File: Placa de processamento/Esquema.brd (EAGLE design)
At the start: 145.1 x 89.8 mm, 12 parts

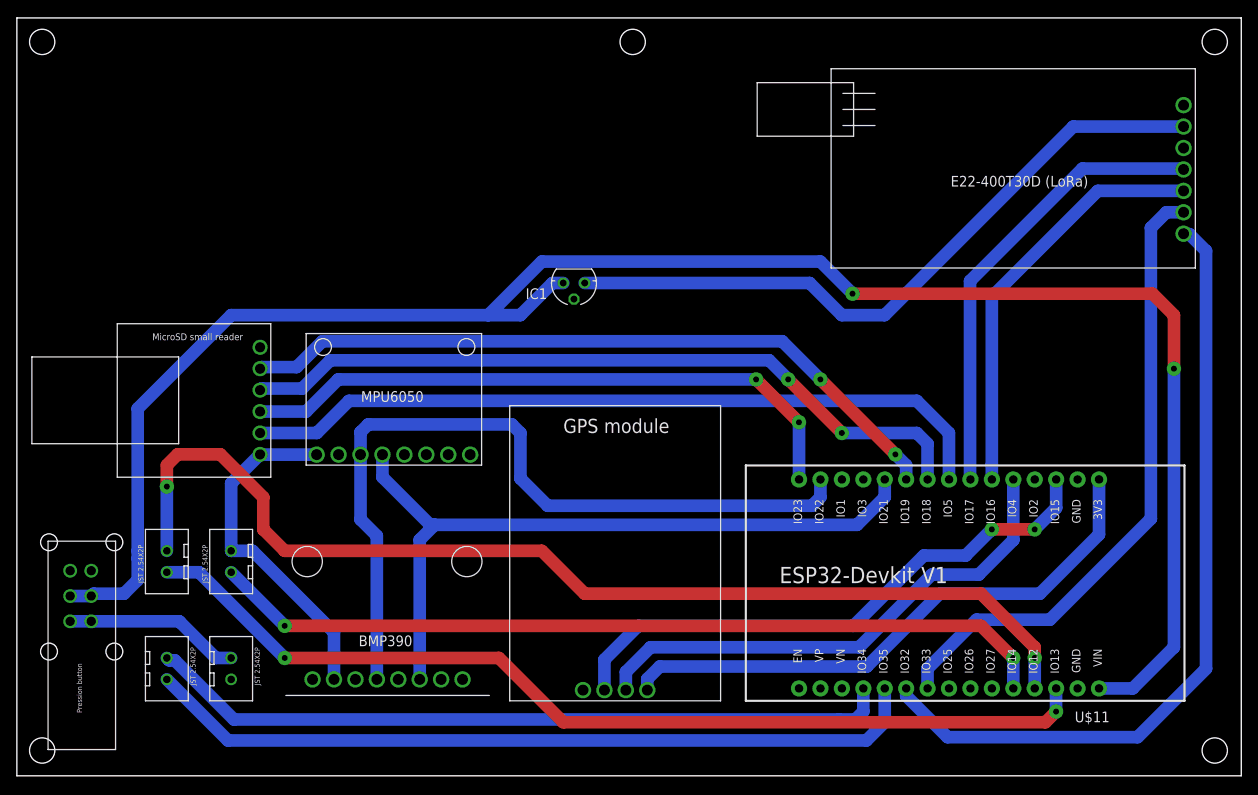
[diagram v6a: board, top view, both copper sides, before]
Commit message: Ajuste de trilhas, furos e posicionamento.
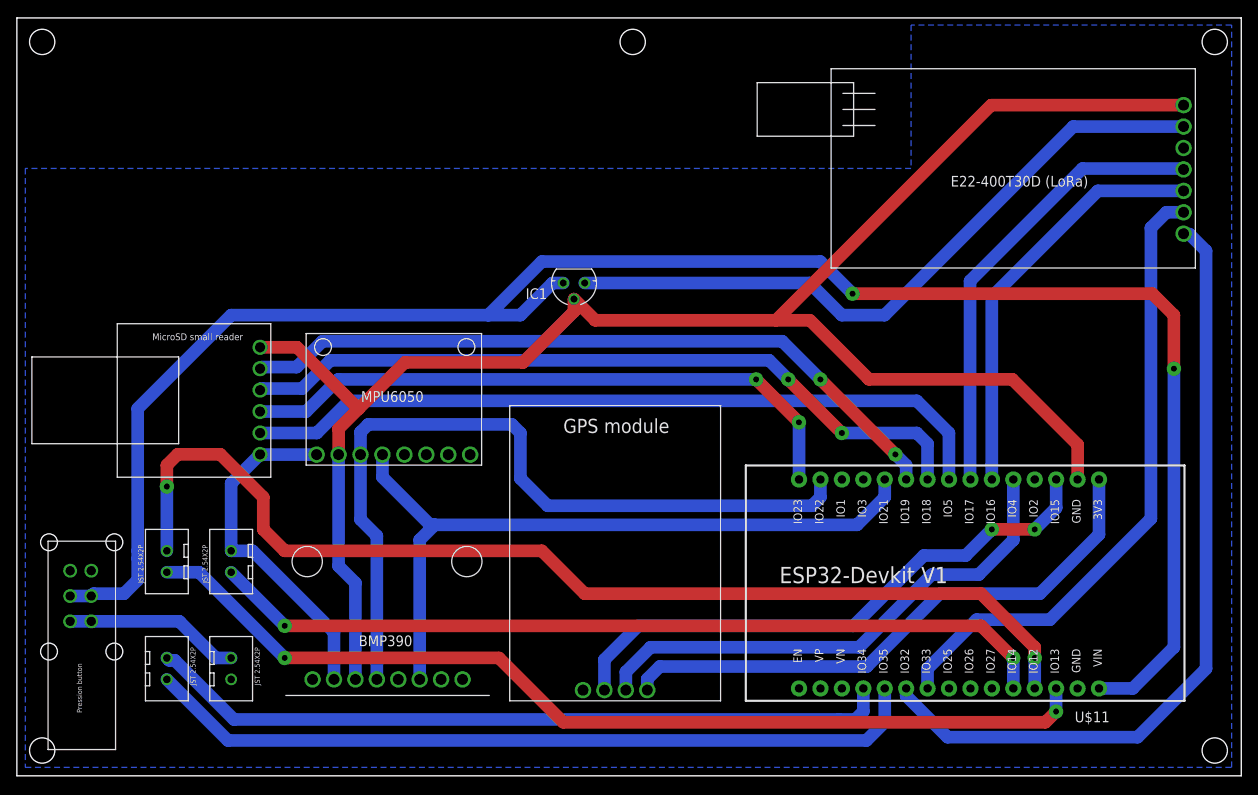
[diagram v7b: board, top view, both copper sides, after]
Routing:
- net N$4: track 0.00 -> 210.2 mm
- added copper zone on layer 16, net GND
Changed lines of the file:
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@@
 <wire x1="145.141" y1="89.84" x2="0" y2="89.84" width="0" layer="20"/>
 <wire x1="0" y1="89.84" x2="0" y2="0" width="0" layer="20"/>
-<dimension x1="0" y1="-3.81" x2="145.161" y2="-3.81" x3="72.5805" y3="-7.62" textsize="1.778" layer="27"/>
-<dimension x1="-2.54" y1="0" x2="-2.54" y2="90.17" x3="-5.08" y3="45.085" textsize="1.778" layer="47"/>
 <hole x="142" y="87" drill="3"/>
 <hole x="142" y="3" drill="3"/>
@@
 <hole x="3" y="87" drill="3"/>
 <hole x="73" y="87" drill="3"/>
+<dimension x1="0" y1="89.84" x2="0" y2="0" x3="-6" y3="44.92" textsize="1.778" layer="21" dtype="vertical"/>
+<dimension x1="0" y1="0" x2="145.141" y2="0" x3="72.5705" y3="-9" textsize="1.778" layer="21" dtype="vertical"/>
 </plain>
 <attributes>
@@
 <contactref element="U$8" pad="GND"/>
 <contactref element="U$2" pad="GND"/>
-<wire x1="125.74" y1="35.13" x2="138.303" y2="79.502" width="0" layer="19" extent="1-1"/>
-<wire x1="66.04" y1="56.515" x2="125.74" y2="35.13" width="0" layer="19" extent="1-1"/>
-<wire x1="38.1355" y1="38.0755" x2="66.04" y2="56.515" width="0" layer="19" extent="1-1"/>
-<wire x1="28.829" y1="50.8" x2="38.1355" y2="38.0755" width="0" layer="19" extent="1-1"/>
-<wire x1="40.132" y1="11.43" x2="38.1355" y2="38.0755" width="0" layer="19" extent="1-1"/>
-<wire x1="67.11" y1="10.16" x2="40.132" y2="11.43" width="0" layer="19" extent="1-1"/>
+<wire x1="66.04" y1="56.515" x2="68.555" y2="54" width="1.5" layer="1"/>
+<wire x1="101" y1="47" x2="118" y2="47" width="1.5" layer="1"/>
+<wire x1="118" y1="47" x2="125.74" y2="39.26" width="1.5" layer="1"/>
+<wire x1="125.74" y1="39.26" x2="125.74" y2="35.13" width="1.5" layer="1"/>
+<wire x1="68.555" y1="54" x2="90" y2="54" width="1.5" layer="1"/>
+<wire x1="90" y1="54" x2="94" y2="54" width="1.5" layer="1"/>
+<wire x1="94" y1="54" x2="101" y2="47" width="1.5" layer="1"/>
+<wire x1="138.303" y1="79.502" x2="115.502" y2="79.502" width="1.5" layer="1"/>
+<wire x1="115.502" y1="79.502" x2="90" y2="54" width="1.5" layer="1"/>
+<wire x1="38.1355" y1="38.0755" x2="38.1355" y2="41.1355" width="1.5" layer="1"/>
+<wire x1="46" y1="49" x2="60" y2="49" width="1.5" layer="1"/>
+<wire x1="60" y1="49" x2="66.04" y2="55.04" width="1.5" layer="1"/>
+<wire x1="66.04" y1="55.04" x2="66.04" y2="56.515" width="1.5" layer="1"/>
+<wire x1="38.1355" y1="41.1355" x2="40.5" y2="43.5" width="1.5" layer="1"/>
+<wire x1="40.5" y1="43.5" x2="46" y2="49" width="1.5" layer="1"/>
+<wire x1="28.829" y1="50.8" x2="33.2" y2="50.8" width="1.5" layer="1"/>
+<wire x1="33.2" y1="50.8" x2="40.5" y2="43.5" width="1.5" layer="1"/>
+<wire x1="38.1355" y1="38.0755" x2="38.1355" y2="24.8645" width="1.5" layer="16"/>
+<wire x1="40.132" y1="22.868" x2="40.132" y2="11.43" width="1.5" layer="16"/>
+<wire x1="38.1355" y1="24.8645" x2="40.132" y2="22.868" width="1.5" layer="16"/>
+<wire x1="40.132" y1="11.43" x2="67.11" y2="10.16" width="0" layer="19" extent="1-1"/>
 </signal>
 <signal name="N$5">
@@
 <contactref element="U$11" pad="29"/>
 <contactref element="U$7" pad="2"/>
+<polygon width="1.5" layer="16">
+<vertex x="1" y="1"/>
+<vertex x="144" y="1"/>
+<vertex x="144" y="89"/>
+<vertex x="106" y="89"/>
+<vertex x="106" y="72"/>
+<vertex x="1" y="72"/>
+</polygon>
 <wire x1="25.4" y1="11.43" x2="125.74" y2="10.36" width="0" layer="19" extent="1-1"/>
 </signal>

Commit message: Ajustes na PCB finalizados!
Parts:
- moved U$10 1.00 mm to (8.62, 16.5)
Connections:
- removed net N$4: IC1.GND, U$1.GND, U$11.2, U$2.GND, U$3.GND, U$8.GND, U$9.GND
- net GND: now also IC1.GND, U$1.GND, U$11.2, U$2.GND, U$3.GND, U$8.GND, U$9.GND
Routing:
- net GND: track 0.00 -> 350.3 mm, vias 0 -> 8
- net N$4: track 210.2 -> 0.00 mm
- net N$3: track 109.8 -> 201.5 mm, vias 0 -> 4
- net N$20: track 130.1 -> 120.8 mm
- net N$7: track 222.5 -> 225.4 mm
- net N$21: track 100.5 -> 101.7 mm
- net V_BATTERY: track 20.9 -> 19.9 mm
